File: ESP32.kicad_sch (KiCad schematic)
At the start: 1 part, among them U1 ESP32-C6-MINI-1/U

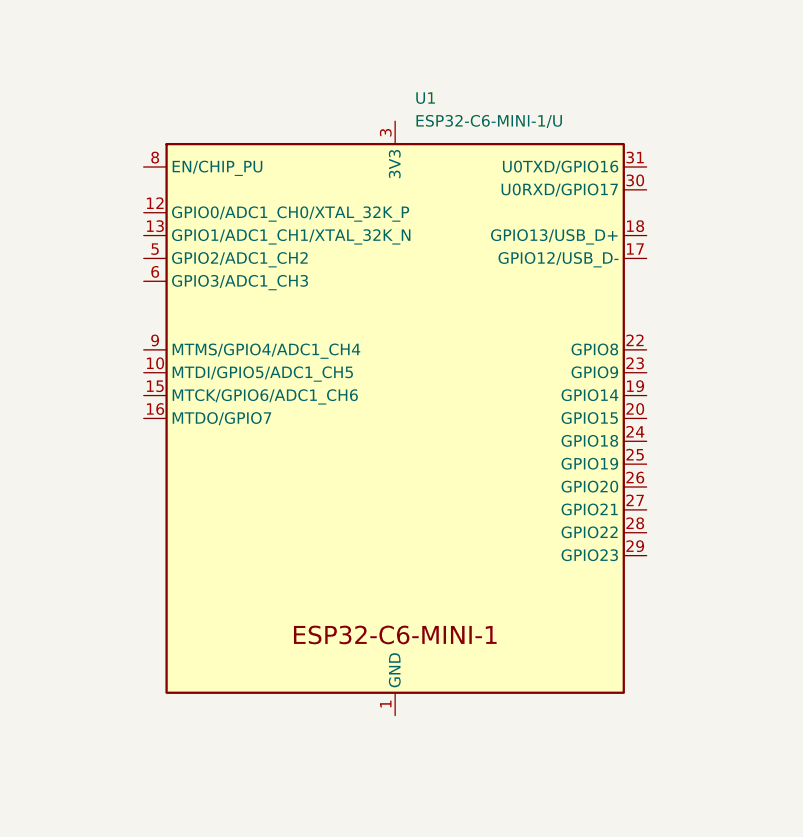
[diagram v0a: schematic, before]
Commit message: added USB-C connector
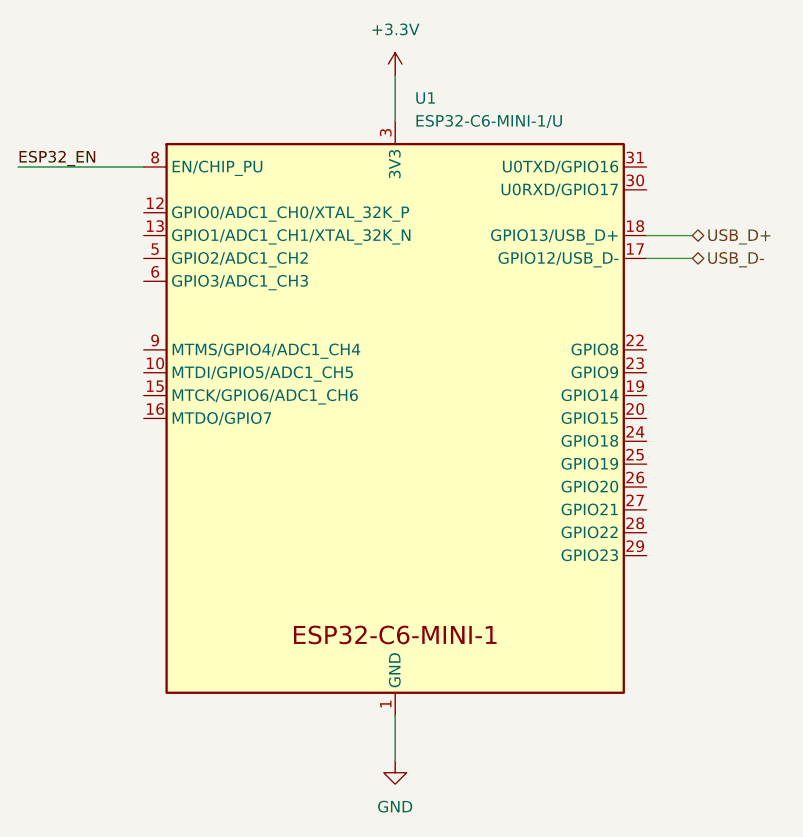
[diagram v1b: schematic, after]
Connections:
- net GND: now reaches U1.1 (GND), U1.11 (GND), U1.14 (GND), U1.2 (GND), U1.36 (GND), U1.37 (GND), U1.38 (GND), U1.39 (GND), U1.40 (GND), U1.41 (GND), U1.42 (GND), U1.43 (GND), U1.44 (GND), U1.45 (GND), U1.46 (GND), U1.47 (GND), U1.48 (GND), U1.49 (GND), U1.50 (GND), U1.51 (GND), U1.52 (GND), U1.53 (GND)
- net USB_D-: now reaches U1.17 (GPIO12/USB_D-)
- net USB_D+: now reaches U1.18 (GPIO13/USB_D+)
- net +3.3V: now reaches U1.3 (3V3)
- net ESP32_EN: now reaches U1.8 (EN/CHIP_PU)
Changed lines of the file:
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@@
 	(generator_version "8.0")
 	(paper "A4")
+	(wire
+		(pts
+			(xy 149.86 129.54) (xy 149.86 134.62)
+		)
+		(stroke
+			(width 0)
+			(type default)
+		)
+	)
+	(wire
+		(pts
+			(xy 177.8 78.74) (xy 182.88 78.74)
+		)
+		(stroke
+			(width 0)
+			(type default)
+		)
+	)
+	(wire
+		(pts
+			(xy 107.95 68.58) (xy 121.92 68.58)
+		)
+		(stroke
+			(width 0)
+			(type default)
+		)
+	)
+	(wire
+		(pts
+			(xy 149.86 58.42) (xy 149.86 63.5)
+		)
+		(stroke
+			(width 0)
+			(type default)
+		)
+	)
+	(wire
+		(pts
+			(xy 177.8 76.2) (xy 182.88 76.2)
+		)
+		(stroke
+			(width 0)
+			(type default)
+		)
+	)
+	(label "ESP32_EN"
+		(at 107.95 68.58 0)
+		(fields_autoplaced yes)
+		(effects
+			(font
+				(size 1.27 1.27)
+			)
+			(justify left bottom)
+		)
+	)
+	(hierarchical_label "USB_D+"
+		(shape bidirectional)
+		(at 182.88 76.2 0)
+		(fields_autoplaced yes)
+		(effects
+			(font
+				(size 1.27 1.27)
+			)
+			(justify left)
+		)
+	)
+	(hierarchical_label "USB_D-"
+		(shape bidirectional)
+		(at 182.88 78.74 0)
+		(fields_autoplaced yes)
+		(effects
+			(font
+				(size 1.27 1.27)
+			)
+			(justify left)
+		)
+	)
 	(symbol
 		(lib_id "PCM_Espressif:ESP32-C6-MINI-1/U")
@@
 					(unit 1)
 				)
+			)
+		)
+	)
+	(symbol
+		(lib_id "power:GND")
+		(at 149.86 134.62 0)
+		(unit 1)
+		(exclude_from_sim no)
+		(in_bom yes)
+		(on_board yes)
+		(dnp no)
+		(fields_autoplaced yes)
+		(property "Reference" "#PWR01"
+			(at 149.86 140.97 0)
+			(effects
+				(font
+					(size 1.27 1.27)
+				)
+				(hide yes)
+			)
+		)
+		(property "Value" "GND"
+			(at 149.86 139.7 0)
+			(effects
+				(font
+					(size 1.27 1.27)
+				)
+			)
+		)
+		(property "Footprint" ""
+			(at 149.86 134.62 0)
+			(effects
+				(font
+					(size 1.27 1.27)
+				)
+				(hide yes)
+			)
+		)
+		(property "Datasheet" ""
+			(at 149.86 134.62 0)
+			(effects
+				(font
+					(size 1.27 1.27)
+				)
+				(hide yes)
+			)
+		)
+		(property "Description" "Power symbol creates a global label with name \"GND\" , ground"
+			(at 149.86 134.62 0)
+			(effects
+				(font
+					(size 1.27 1.27)
+				)
+				(hide yes)
+			)
+		)
+		(pin "1"
+		)
+		(instances
+			(project ""
+				(path "/0204cec0-d71e-48a7-8736-ccb0d3e9b02c/800114ef-aa85-4b1c-8a44-880992c7295f"
+					(reference "#PWR01")
+					(unit 1)
+				)
+			)
+		)
+	)
+	(symbol
+		(lib_id "power:+3.3V")
+		(at 149.86 58.42 0)
+		(unit 1)
+		(exclude_from_sim no)
+		(in_bom yes)
+		(on_board yes)
+		(dnp no)
+		(fields_autoplaced yes)
+		(property "Reference" "#PWR02"
+			(at 149.86 62.23 0)
+			(effects
+				(font
+					(size 1.27 1.27)
+				)
+				(hide yes)
+			)
+		)
+		(property "Value" "+3.3V"
+			(at 149.86 53.34 0)
+			(effects
+				(font
+					(size 1.27 1.27)
+				)
+			)
+		)
+		(property "Footprint" ""
+			(at 149.86 58.42 0)
+			(effects
+				(font
+					(size 1.27 1.27)
+				)
+				(hide yes)
+			)
+		)
+		(property "Datasheet" ""
+			(at 149.86 58.42 0)
+			(effects
+				(font
+					(size 1.27 1.27)
+				)
+				(hide yes)
+			)
+		)
+		(property "Description" "Power symbol creates a global label with name \"+3.3V\""
+			(at 149.86 58.42 0)
+			(effects
+				(font
+					(size 1.27 1.27)
+				)
+				(hide yes)
+			)
+		)
+		(pin "1"
+		)
+		(instances
+			(project ""
+				(path "/0204cec0-d71e-48a7-8736-ccb0d3e9b02c/800114ef-aa85-4b1c-8a44-880992c7295f"
+					(reference "#PWR02")
+					(unit 1)
+				)

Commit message: USB and PWR sch
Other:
- title: (none) -> ESP32
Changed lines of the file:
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@@
 	(generator_version "8.0")
 	(paper "A4")
+	(title_block
+		(title "ESP32")
+	)
 	(wire
 		(pts

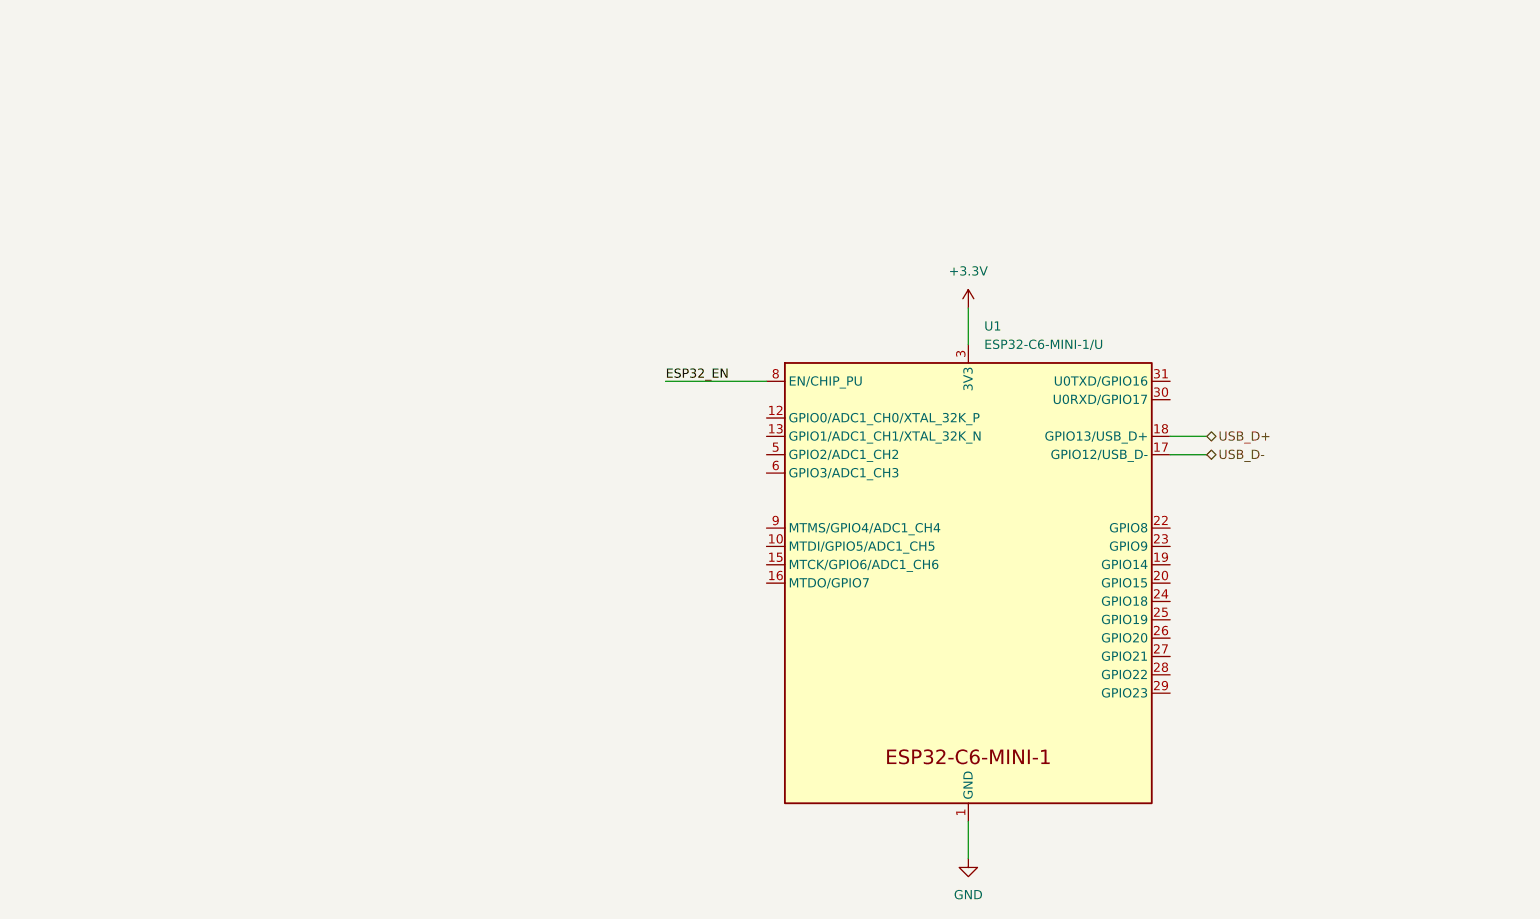
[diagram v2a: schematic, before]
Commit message: add BOOT/RST switches
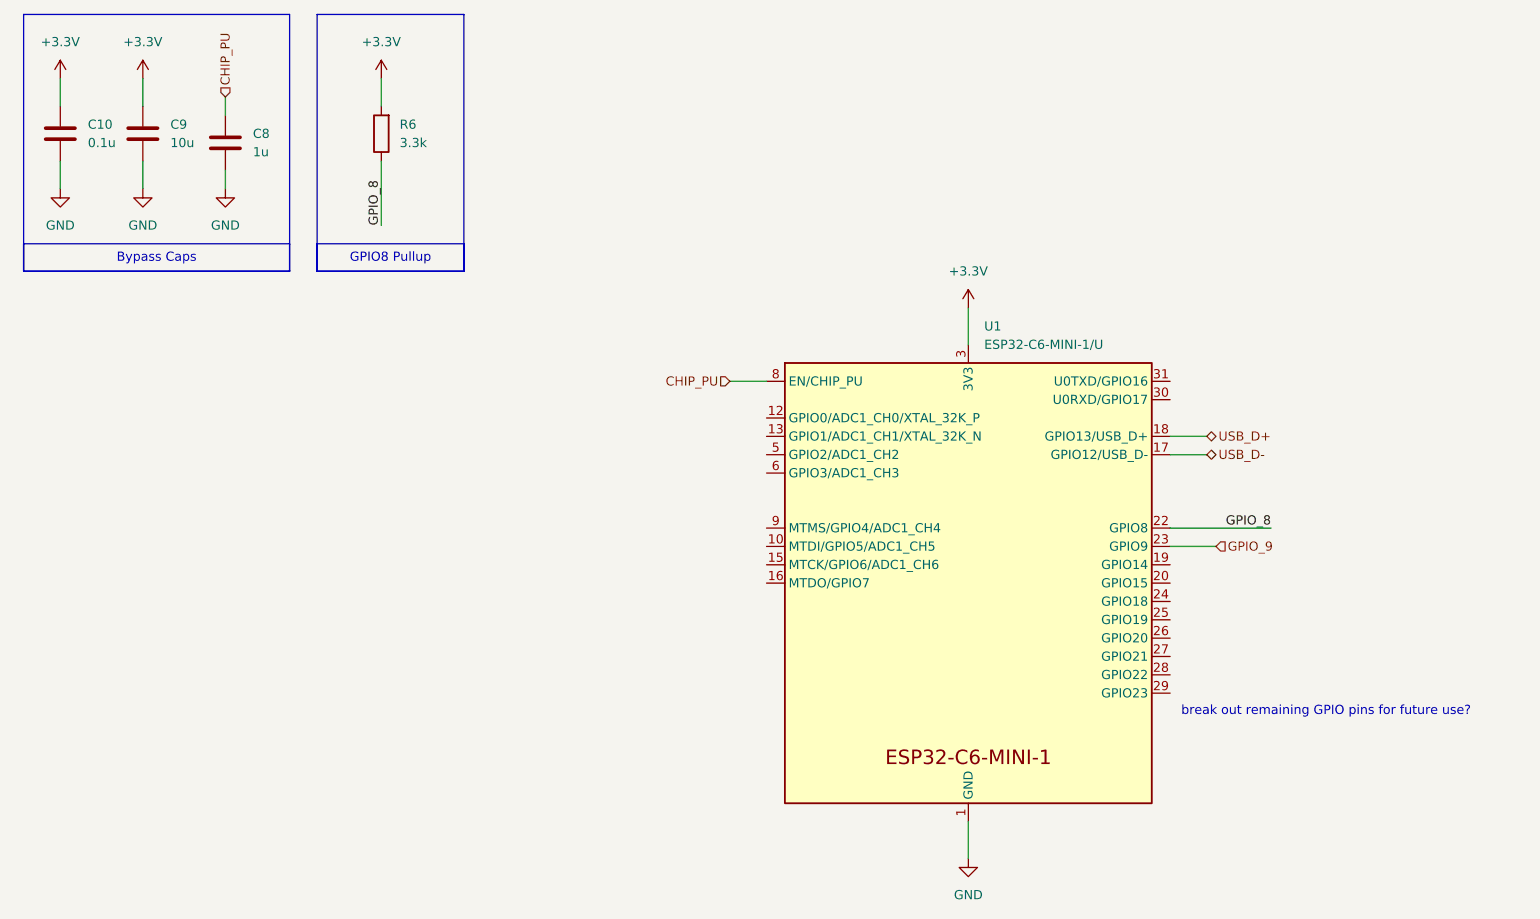
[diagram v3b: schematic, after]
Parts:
- added C10: 0.1u, symbol Device:C
- added C8: 1u, symbol Device:C
- added C9: 10u, symbol Device:C
- added R6: 3.3k, symbol Device:R
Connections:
- net +3.3V: now also C10.1, C9.1, R6.2
- net GND: now also C10.2, C8.2, C9.2
- net GPIO_8: now reaches U1.22 (GPIO8)
- net GPIO_8: now also R6.1
- net GPIO_9: now reaches U1.23 (GPIO9)
- net ESP32_EN renamed CHIP_PU
- net CHIP_PU: now also C8.1
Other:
- note added: "break out remaining GPIO pins for future use?"

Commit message: finished sch? (need P/Ns)
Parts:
- added J2: CA, symbol Connector:Conn_01x02_Socket
- added J3: CB, symbol Connector:Conn_01x03_Socket
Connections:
- net GPIO_0: now reaches U1.12 (GPIO0/ADC1_CH0/XTAL_32K_P)
- net GPIO_0: now also J2.1 (Pin_1)
- net GPIO_1: now reaches U1.13 (GPIO1/ADC1_CH1/XTAL_32K_N)
- net GPIO_1: now also J2.2 (Pin_2)
- net GPIO_14: now reaches U1.19 (GPIO14)
- net GPIO_15: now reaches U1.20 (GPIO15)
- net GPIO_18: now reaches U1.24 (GPIO18)
- net GPIO_21: now reaches U1.27 (GPIO21)
- net GPIO_21: now also J3.3 (Pin_3)
- net GPIO_22: now reaches U1.28 (GPIO22)
- net GPIO_22: now also J3.2 (Pin_2)
- net GPIO_23: now reaches U1.29 (GPIO23)
- net GPIO_23: now also J3.1 (Pin_1)
- no-connect marks 0 -> 10
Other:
- note removed: "break out remaining GPIO pins for future use?"
- moved on the sheet: C10, C8, C9, R6, U1

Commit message: add P/N
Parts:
- C10: P/N (none) -> C0603G104K5RACT250
- C8: P/N (none) -> C0603X105J4RAC7411
- C9: P/N (none) -> MLAST168BB5106MTNA01
- J2: P/N (none) -> 54101-S0802LF
- J3: P/N (none) -> 54101-S0803LF
- R6: P/N (none) -> ERA-3APB332V
- U1: P/N (none) -> ESP32-C6-MINI-1/U
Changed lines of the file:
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@@
+			)
+		)
+		(property "P/N" "54101-S0803LF "
+			(at 74.93 30.48 0)
+			(effects
+				(font
+					(size 1.27 1.27)
+				)
+				(hide yes)
 			)
 		)
@@
 			)
 		)
+		(property "P/N" "ESP32-C6-MINI-1/U"
+			(at 104.14 90.17 0)
+			(effects
+				(font
+					(size 1.27 1.27)
+				)
+				(hide yes)
+			)
+		)
 		(pin "11"
 		)
@@
 			)
 		)
+		(property "P/N" "C0603G104K5RACT250"
+			(at 22.86 73.66 0)
+			(effects
+				(font
+					(size 1.27 1.27)
+				)
+				(hide yes)
+			)
+		)
 		(pin "2"
 		)
@@
 			)
 		)
+		(property "P/N" "MLAST168BB5106MTNA01"
+			(at 34.29 73.66 0)
+			(effects
+				(font
+					(size 1.27 1.27)
+				)
+				(hide yes)
+			)
+		)
 		(pin "2"
 		)
@@
 			)
 		)
+		(property "P/N" "ERA-3APB332V "
+			(at 43.18 34.29 0)
+			(effects
+				(font
+					(size 1.27 1.27)
+				)
+				(hide yes)
+			)
+		)
 		(pin "2"
 		)
@@
 			)
 		)
+		(property "P/N" "54101-S0802LF"
+			(at 74.93 21.59 0)
+			(effects
+				(font
+					(size 1.27 1.27)
+				)
+				(hide yes)
+			)
+		)
 		(pin "2"
 		)
@@
 			(at 45.72 74.93 0)
 			(effects
+				(font
+					(size 1.27 1.27)
+				)
+				(hide yes)
+			)
+		)
+		(property "P/N" "C0603X105J4RAC7411"
+			(at 45.72 74.93 0)
+			(effects

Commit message: assign footprints
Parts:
- C10, C8, C9: footprint (none) -> Capacitor_SMD:C_0603_1608Metric
- J2: footprint (none) -> Connector_PinHeader_2.54mm:PinHeader_1x02_P2.54mm_Vertical
- J3: footprint (none) -> Connector_PinHeader_2.54mm:PinHeader_1x03_P2.54mm_Vertical
- R6: footprint (none) -> Resistor_SMD:R_0603_1608Metric
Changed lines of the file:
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@@
 			)
 		)
-		(property "Footprint" ""
+		(property "Footprint" "Connector_PinHeader_2.54mm:PinHeader_1x03_P2.54mm_Vertical"
 			(at 74.93 30.48 0)
 			(effects
@@
 			)
 		)
-		(property "Footprint" ""
+		(property "Footprint" "Capacitor_SMD:C_0603_1608Metric"
 			(at 23.8252 77.47 0)
 			(effects
@@
 			)
 		)
-		(property "Footprint" ""
+		(property "Footprint" "Capacitor_SMD:C_0603_1608Metric"
 			(at 35.2552 77.47 0)
 			(effects
@@
 			)
 		)
-		(property "Footprint" ""
+		(property "Footprint" "Resistor_SMD:R_0603_1608Metric"
 			(at 44.958 34.29 90)
 			(effects
@@
 			)
 		)
-		(property "Footprint" ""
+		(property "Footprint" "Connector_PinHeader_2.54mm:PinHeader_1x02_P2.54mm_Vertical"
 			(at 74.93 21.59 0)
 			(effects
@@
 			)
 		)
-		(property "Footprint" ""
+		(property "Footprint" "Capacitor_SMD:C_0603_1608Metric"
 			(at 46.6852 78.74 0)
 			(effects

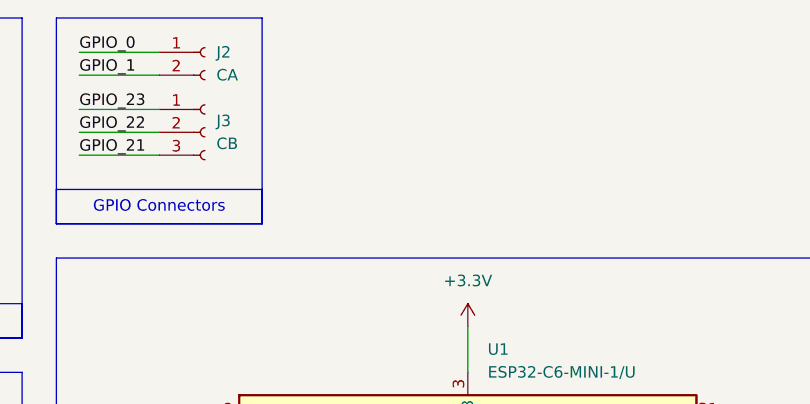
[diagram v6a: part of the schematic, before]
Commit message: readme, mounting holes, minor silk changes
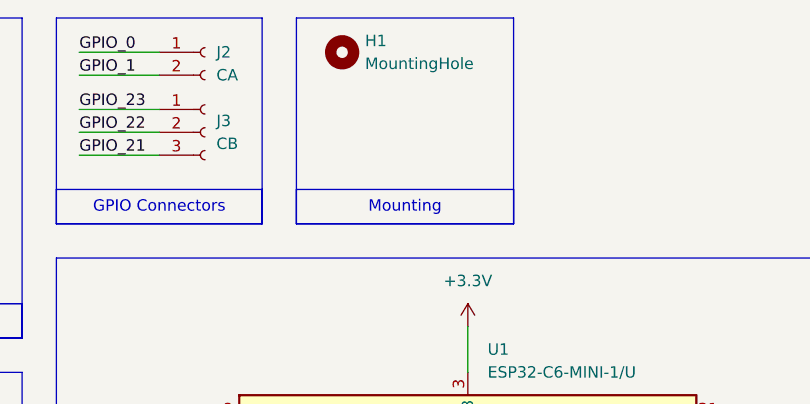
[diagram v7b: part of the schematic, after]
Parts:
- added H1: MountingHole, MountingHole:MountingHole_2.2mm_M2, symbol Mechanical:MountingHole
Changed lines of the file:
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@@
+	)
+	(rectangle
+		(start 85.09 17.78)
+		(end 109.22 40.64)
+		(stroke
+			(width 0)
+			(type default)
+		)
+		(fill
+			(type none)
+		)
 	)
 	(rectangle
@@
 		(at 58.42 137.16 0)
 		(size 92.71 3.81)
+		(stroke
+			(width 0)
+			(type default)
+		)
+		(fill
+			(type none)
+		)
+		(effects
+			(font
+				(size 1.27 1.27)
+			)
+			(justify top)
+		)
+	)
+	(text_box "Mounting"
+		(exclude_from_sim no)
+		(at 85.09 36.83 0)
+		(size 24.13 3.81)
 		(stroke
 			(width 0)
@@
 					(unit 1)
 				)
+			)
+		)
+	)
+	(symbol
+		(lib_id "Mechanical:MountingHole")
+		(at 90.17 21.59 0)
+		(unit 1)
+		(exclude_from_sim yes)
+		(in_bom no)
+		(on_board yes)
+		(dnp no)
+		(fields_autoplaced yes)
+		(property "Reference" "H1"
+			(at 92.71 20.3199 0)
+			(effects
+				(font
+					(size 1.27 1.27)
+				)
+				(justify left)
+			)
+		)
+		(property "Value" "MountingHole"
+			(at 92.71 22.8599 0)
+			(effects
+				(font
+					(size 1.27 1.27)
+				)
+				(justify left)
+			)
+		)
+		(property "Footprint" "MountingHole:MountingHole_2.2mm_M2"
+			(at 90.17 21.59 0)
+			(effects
+				(font
+					(size 1.27 1.27)
+				)
+				(hide yes)
+			)
+		)
+		(property "Datasheet" "~"
+			(at 90.17 21.59 0)
+			(effects
+				(font
+					(size 1.27 1.27)
+				)
+				(hide yes)
+			)
+		)
+		(property "Description" "Mounting Hole without connection"
+			(at 90.17 21.59 0)
+			(effects
+				(font
+					(size 1.27 1.27)
+				)
+				(hide yes)
+			)
+		)
+		(instances
+			(project ""
+				(path "/0204cec0-d71e-48a7-8736-ccb0d3e9b02c/800114ef-aa85-4b1c-8a44-880992c7295f"
+					(reference "H1")
+					(unit 1)
+				)

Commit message: switch caps for lower cost
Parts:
- C10: P/N C0603G104K5RACT250 -> UMK107B7104KAHT
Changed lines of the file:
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@@
 			)
 		)
-		(property "P/N" "C0603G104K5RACT250"
+		(property "P/N" "UMK107B7104KAHT "
 			(at 22.86 73.66 0)
 			(effects
